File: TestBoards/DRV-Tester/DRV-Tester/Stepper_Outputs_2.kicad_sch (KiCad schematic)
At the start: 2 parts, among them J5 Screw_Terminal_01x02, J6 Screw_Terminal_01x02

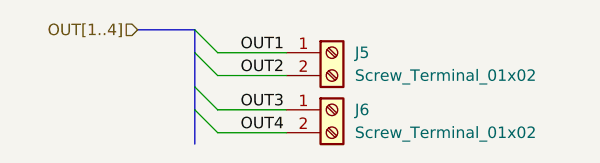
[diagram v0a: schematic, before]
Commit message: update tester board with layout
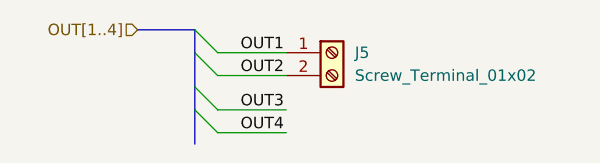
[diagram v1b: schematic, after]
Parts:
- removed J6: Screw_Terminal_01x02, easyeda2kicad:CONN-TH_P5.08_KF128-5.08-2P, symbol Connector:Screw_Terminal_01x02
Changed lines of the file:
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@@
+		)
+	)
+	(wire
+		(pts
+			(xy 77.47 76.2) (xy 85.09 76.2)
+		)
+		(stroke
+			(width 0)
+			(type default)
 		)
 	)
@@
 		)
 	)
+	(bus
+		(pts
+			(xy 74.93 73.66) (xy 74.93 77.47)
+		)
+		(stroke
+			(width 0)
+			(type default)
+		)
+	)
+	(wire
+		(pts
+			(xy 77.47 73.66) (xy 85.09 73.66)
+		)
+		(stroke
+			(width 0)
+			(type default)
+		)
+	)
 	(wire
 		(pts
@@
 		)
 	)
+	(bus
+		(pts
+			(xy 68.58 64.77) (xy 74.93 64.77)
+		)
+		(stroke
+			(width 0)
+			(type default)
+		)
+	)
 	(wire
 		(pts
 			(xy 77.47 69.85) (xy 85.09 69.85)
-		)
-		(stroke
-			(width 0)
-			(type default)
-		)
-	)
-	(bus
-		(pts
-			(xy 74.93 73.66) (xy 74.93 77.47)
-		)
-		(stroke
-			(width 0)
-			(type default)
-		)
-	)
-	(bus
-		(pts
-			(xy 68.58 64.77) (xy 74.93 64.77)
-		)
-		(stroke
-			(width 0)
-			(type default)
-		)
-	)
-	(wire
-		(pts
-			(xy 77.47 73.66) (xy 85.09 73.66)
-		)
-		(stroke
-			(width 0)
-			(type default)
-		)
-	)
-	(wire
-		(pts
-			(xy 77.47 76.2) (xy 85.09 76.2)
 		)
 		(stroke
@@
 		(instances
 			(project "DRV-Tester"
+				(path "/a38efaf2-f631-4fae-9db8-baf53fe35d9e/65a6da3d-ab5d-45b9-ade3-98df1f09408e"
+					(reference "J3")
+					(unit 1)
+				)
+				(path "/a38efaf2-f631-4fae-9db8-baf53fe35d9e/69746995-a133-4aa1-9a0a-8be4c0d0a678"
+					(reference "J1")
+					(unit 1)
+				)
 				(path "/a38efaf2-f631-4fae-9db8-baf53fe35d9e/6fce963f-344a-41d8-afb4-08884e66bd5a"
 					(reference "J5")
 					(unit 1)
 				)
-			)
-		)
-	)
-	(symbol
-		(lib_id "Connector:Screw_Terminal_01x02")
-		(at 90.17 73.66 0)
-		(unit 1)
-		(exclude_from_sim no)
-		(in_bom yes)
-		(on_board yes)
-		(dnp no)
-		(property "Reference" "J6"
-			(at 92.71 73.6599 0)
-			(effects
-				(font
-					(size 1.27 1.27)
-				)
-				(justify left)
-			)
-		)
-		(property "Value" "Screw_Terminal_01x02"
-			(at 92.71 76.1999 0)
-			(effects
-				(font
-					(size 1.27 1.27)
-				)
-				(justify left)
-			)
-		)
-		(property "Footprint" "easyeda2kicad:CONN-TH_P5.08_KF128-5.08-2P"
-			(at 90.17 73.66 0)
-			(effects
-				(font
-					(size 1.27 1.27)
-				)
-				(hide yes)
-			)
-		)
-		(property "Datasheet" "~"
-			(at 90.17 73.66 0)
-			(effects
-				(font
-					(size 1.27 1.27)
-				)
-				(hide yes)
-			)
-		)
-		(property "Description" "Generic screw terminal, single row, 01x02, script generated (kicad-library-utils/schlib/autogen/connector/)"
-			(at 90.17 73.66 0)
-			(effects
-				(font
-					(size 1.27 1.27)
-				)
-				(hide yes)
-			)
-		)
-		(property "LCSC" "C474952"
-			(at 90.17 73.66 0)
-			(effects
-				(font
-					(size 1.27 1.27)
-				)
-				(hide yes)
-			)
-		)
-		(property "LCSC Part" "C474952"
-			(at 90.17 73.66 0)
-			(effects
-				(font
-					(size 1.27 1.27)
-				)
-				(hide yes)
-			)
-		)
-		(property "LCSC Part Number" "C474952"
-			(at 90.17 73.66 0)
-			(effects
-				(font
-					(size 1.27 1.27)
-				)
-				(hide yes)
-			)
-		)
-		(pin "2"
-		)
-		(pin "1"
-		)
-		(instances
-			(project "DRV-Tester"
-				(path "/a38efaf2-f631-4fae-9db8-baf53fe35d9e/6fce963f-344a-41d8-afb4-08884e66bd5a"
-					(reference "J6")
-					(unit 1)
-				)

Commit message: add caps and LEDs to testboard
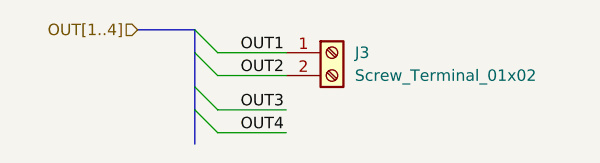
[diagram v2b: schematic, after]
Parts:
- renumbered J5 to J3
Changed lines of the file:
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@@
 		(on_board yes)
 		(dnp no)
-		(property "Reference" "J5"
+		(property "Reference" "J3"
 			(at 92.71 67.3099 0)
 			(effects
@@
 					(unit 1)
 				)
-				(path "/a38efaf2-f631-4fae-9db8-baf53fe35d9e/6fce963f-344a-41d8-afb4-08884e66bd5a"
-					(reference "J5")
-					(unit 1)
-				)
